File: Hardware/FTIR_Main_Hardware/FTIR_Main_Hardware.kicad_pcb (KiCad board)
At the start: 2 copper layers, 85.9 x 53.1 mm, 52 parts, among them J1 RJ45_LED_Shielded, Q1 IRF7606PBF, Q2 BSS138, Q3 IRF7606PBF, Q4 IRF7606PBF, Q5 BSS138, Q6 BSS138, U2 D36V28F7, U3 OKI, U4 TMC2208_Breakout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

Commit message: Added a few traces
I have an 8 AM class in 5 hours :(
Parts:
- C1, C2, C4, C5: moved to B.Cu
- moved C5 9.42 mm to (133.6, 82.8)
- moved C1 6.41 mm to (121.2, 82.8), turned to 180 degrees
- moved C4 6.24 mm to (133.6, 87.9), turned to 0 degrees
- moved C2 5.05 mm to (121.2, 87.9)
- moved R12 0.61 mm to (134.4, 78.3)
- moved Q2 0.48 mm to (131.3, 78.3)
- moved R11 0.48 mm to (128.3, 76.0), turned to -90 degrees
- moved R10 0.48 mm to (131.2, 75.1)
- moved Q1 0.46 mm to (130.1, 70.2)
- moved D9 0.45 mm to (144.3, 72.3)
- moved R19 0.45 mm to (144.3, 68.5)
- moved R21 0.35 mm to (144.2, 78.5)
- moved R9 0.29 mm to (134.2, 68.5)
- moved D7 0.29 mm to (134.2, 72.3)
- moved D10 0.29 mm to (154.4, 72.2)
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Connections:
- Conn1 pad 2: (no net) -> +12V
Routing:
- net +12V: track 0.00 -> 96.5 mm
- net +7.5V: track 0.00 -> 93.6 mm, vias 0 -> 1
- net +5V: track 0.00 -> 68.0 mm
- net T-: track 0.00 -> 54.3 mm
- net T+: track 0.00 -> 54.2 mm
- net R+: track 0.00 -> 53.5 mm
- net R-: track 0.00 -> 53.4 mm
- net +3V3: track 0.00 -> 39.8 mm
- net Net-(Conn12-Pad1): track 0.00 -> 11.1 mm
- net Net-(Conn6-Pad1): track 0.00 -> 10.9 mm
- net Net-(C3-Pad1): track 0.00 -> 10.6 mm
- net Net-(Conn11-Pad1): track 0.00 -> 10.3 mm
- net Net-(Conn4-Pad4): track 0.00 -> 10.3 mm
- net Net-(Conn4-Pad1): track 0.00 -> 10.3 mm
- net Net-(Conn4-Pad3): track 0.00 -> 10.3 mm
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
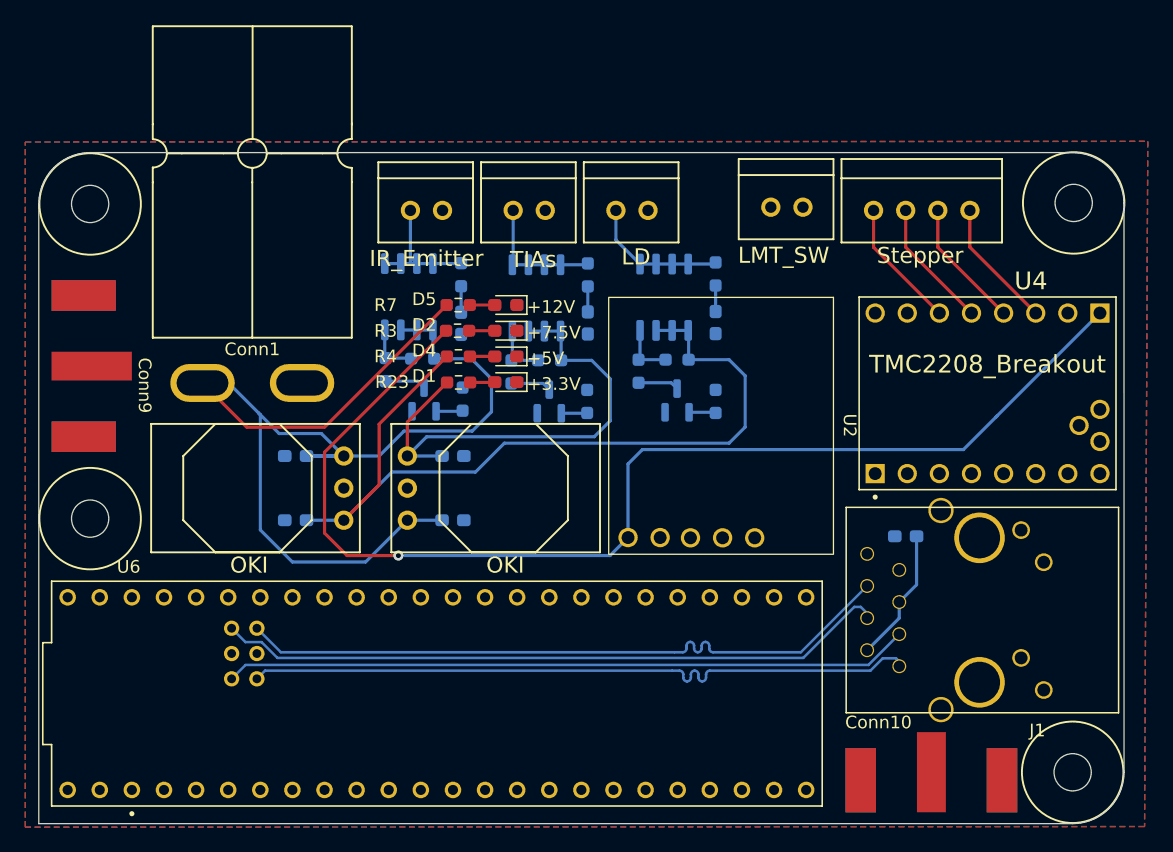
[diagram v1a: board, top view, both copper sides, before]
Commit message: More trace routing
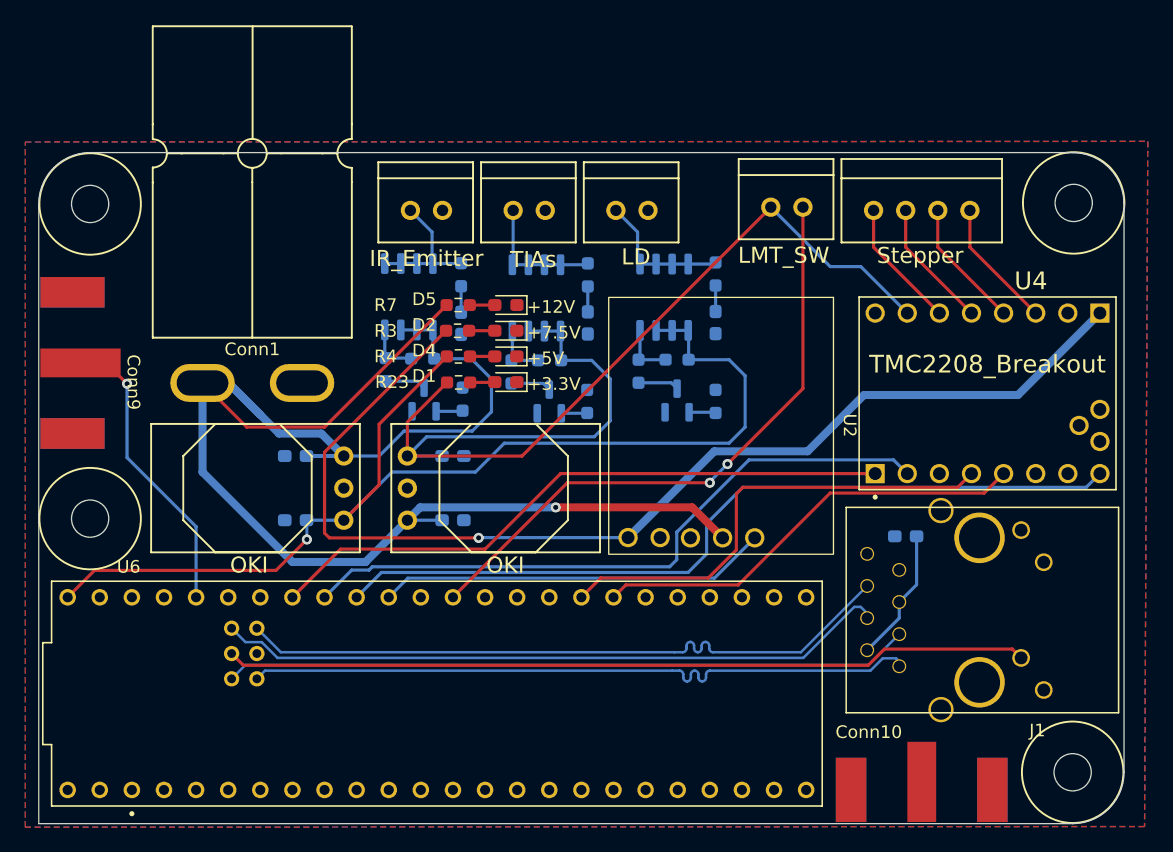
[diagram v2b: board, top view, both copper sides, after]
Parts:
- moved Conn10 1.08 mm to (170.7, 109.2)
- moved Conn9 0.92 mm to (103.5, 75.4)
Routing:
- net DRIVER_EN: track 0.00 -> 64.3 mm
- net ETH_LED: track 0.00 -> 63.7 mm
- net STEP: track 0.00 -> 52.3 mm
- net +3V3: track 39.8 -> 90.9 mm
- net DIR: track 0.00 -> 50.2 mm
- net Net-(U6-A0): track 0.00 -> 48.9 mm, vias 0 -> 2
- net PDN: track 0.00 -> 37.5 mm
- net +12V: track 96.5 -> 132.9 mm, vias 0 -> 1
- net UART: track 0.00 -> 34.9 mm
- net BUCK_EN: track 0.00 -> 30.9 mm
- net Net-(Conn9-Tip): track 0.00 -> 23.5 mm, vias 0 -> 1
- net +5V: track 68.0 -> 90.4 mm, vias 0 -> 1
- net +7.5V: track 93.6 -> 88.9 mm

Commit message: Finished the board
Added traces and reassigned pins
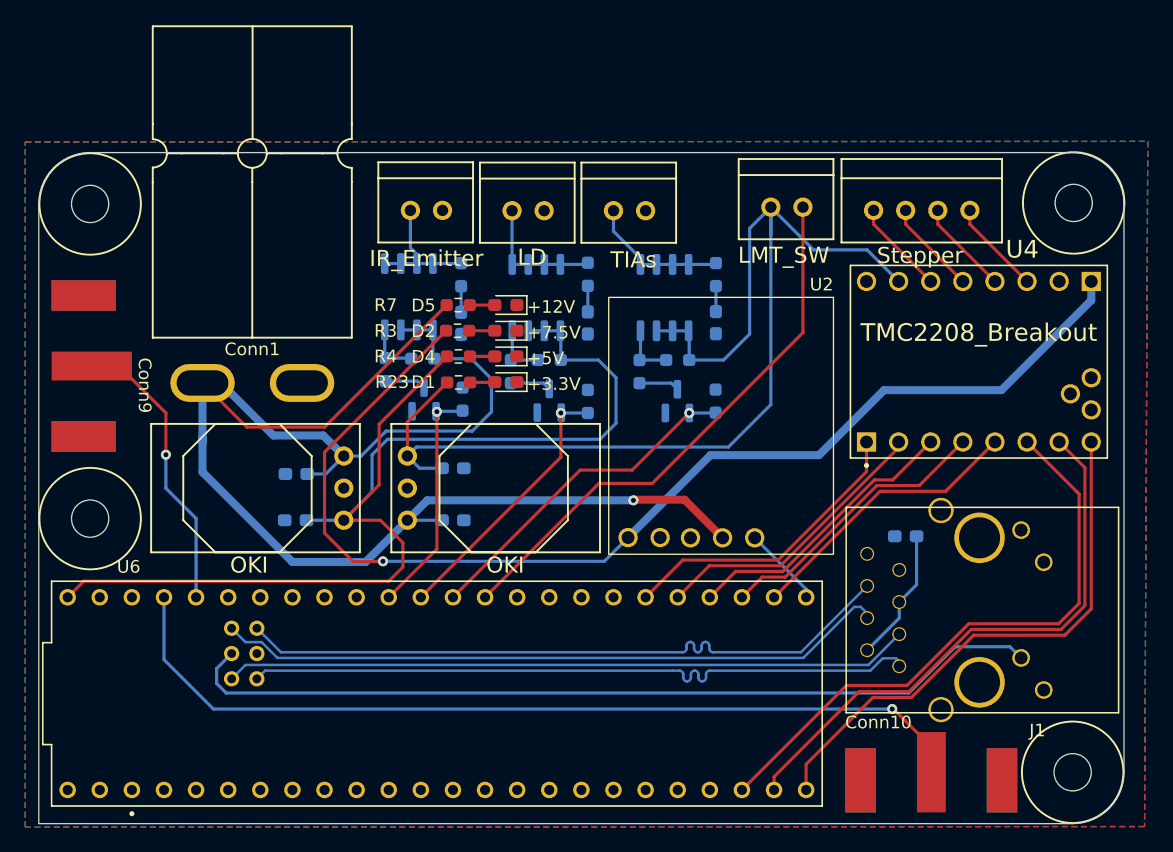
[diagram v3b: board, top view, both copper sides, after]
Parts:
- moved R21 10.2 mm to (154.4, 78.5)
- moved D9 10.1 mm to (154.4, 72.3)
- moved Q5 10.1 mm to (151.4, 78.5)
- moved R19 10.1 mm to (154.4, 68.5)
- moved Q3 10.1 mm to (150.3, 70.3)
- moved R15 10.1 mm to (151.4, 75.2)
- moved R17 10.1 mm to (148.4, 76.1)
- moved D10 10.1 mm to (144.3, 72.3)
- moved Q6 10.1 mm to (141.2, 78.4)
- moved R16 10.1 mm to (141.2, 75.2)
- moved R18 10.1 mm to (138.2, 76.1)
- moved R20 10.1 mm to (144.3, 68.4)
- moved Q4 10.1 mm to (140.2, 70.3)
- moved R22 10.1 mm to (144.3, 78.5)
- moved Conn12 8.22 mm to (138.3, 63.4)
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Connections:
- Conn1 pad 2: +12V -> (no net)
- Conn8 pad 2: Net-(U6-A0) -> Net-(U6-SCK)
- U6 pad 0: LAMP_CTRL -> unconnected-(U6-RX1-Pad0)
- U6 pad 1: MS1_CTRL -> unconnected-(U6-TX1-Pad1)
- U6 pad 13: unconnected-(U6-SCK-Pad13) -> Net-(U6-SCK)
- U6 pad 14: Net-(U6-A0) -> TIA_CTRL
- U6 pad 15: unconnected-(U6-A1-Pad15) -> LD_CTRL
- U6 pad 16: BUCK_EN -> LAMP_CTRL
- U6 pad 17: DRIVER_EN -> unconnected-(U6-A3-Pad17)
- U6 pad 18: STEP -> unconnected-(U6-A4-Pad18)
- U6 pad 19: DIR -> unconnected-(U6-A5-Pad19)
- U6 pad 2: MS2_CTRL -> unconnected-(U6-OUT2-Pad2)
- U6 pad 28: CLK -> unconnected-(U6-RX7-Pad28)
- U6 pad 30: unconnected-(U6-CRX3-Pad30) -> MS2_CTRL
- U6 pad 31: unconnected-(U6-CTX3-Pad31) -> MS1_CTRL
- U6 pad 32: unconnected-(U6-OUT1B-Pad32) -> DRIVER_EN
- U6 pad 33: unconnected-(U6-MCLK2-Pad33) -> BUCK_EN
- U6 pad 34: unconnected-(U6-RX8-Pad34) -> UART
- U6 pad 35: unconnected-(U6-TX8-Pad35) -> UART
- U6 pad 36: unconnected-(U6-CS2-Pad36) -> CLK
- U6 pad 37: unconnected-(U6-CS3-Pad37) -> STEP
- U6 pad 38: unconnected-(U6-A14-Pad38) -> DIR
- U6 pad 39: UART -> unconnected-(U6-A15-Pad39)
- U6 pad 40: PDN -> unconnected-(U6-A16-Pad40)
- U6 pad 7: TIA_CTRL -> unconnected-(U6-RX2-Pad7)
- U6 pad 8: LD_CTRL -> unconnected-(U6-TX2-Pad8)
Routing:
- net Net-(Conn10-Tip): track 0.00 -> 70.5 mm, vias 0 -> 1
- net Net-(U6-A0): track 48.9 -> 0.00 mm, vias 2 -> 0
- net MS2_CTRL: track 0.00 -> 47.3 mm
- net MS1_CTRL: track 0.00 -> 45.0 mm
- net Net-(U6-SCK): track 0.00 -> 43.7 mm
- net PDN: track 37.5 -> 0.00 mm
- net STEP: track 52.3 -> 22.8 mm
- net DIR: track 50.2 -> 23.9 mm
- net TIA_CTRL: track 2.06 -> 26.8 mm, vias 0 -> 1
- net BUCK_EN: track 30.9 -> 6.39 mm
- net CLK: track 0.00 -> 22.6 mm
- net DRIVER_EN: track 64.3 -> 42.9 mm
- net LD_CTRL: track 2.12 -> 21.4 mm, vias 0 -> 1
- net LAMP_CTRL: track 2.12 -> 18.4 mm, vias 0 -> 1
- net UART: track 34.9 -> 45.1 mm
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
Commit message: Finishing touches on all boards
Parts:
- added G***: LOGO, LOGO, B.Cu at (159.8, 73.5)
- added G***: LOGO, LOGO, B.Cu at (118.0, 69.7)
- added G***: LOGO, LOGO, B.Cu at (147.5, 91.7)
- moved Conn9 0.89 mm to (103.5, 75.7)
- moved Conn10 0.64 mm to (171.4, 109.1)
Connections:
- Conn1 pad 2: (no net) -> +12V
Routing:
- net unconnected-(U6-3.3V-Pad3.3V_1): track 0.00 -> 39.9 mm
- net +12V: track 132.0 -> 127.7 mm
- net Net-(Conn10-Tip): track 70.5 -> 73.2 mm
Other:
- board text added: "7.5v Buck"
- board text added: "FTIR Spectrometer, Rev1 Mars Rover Design Team Missouri S&T, 2024 Drew Wellen and Adam Klassen"

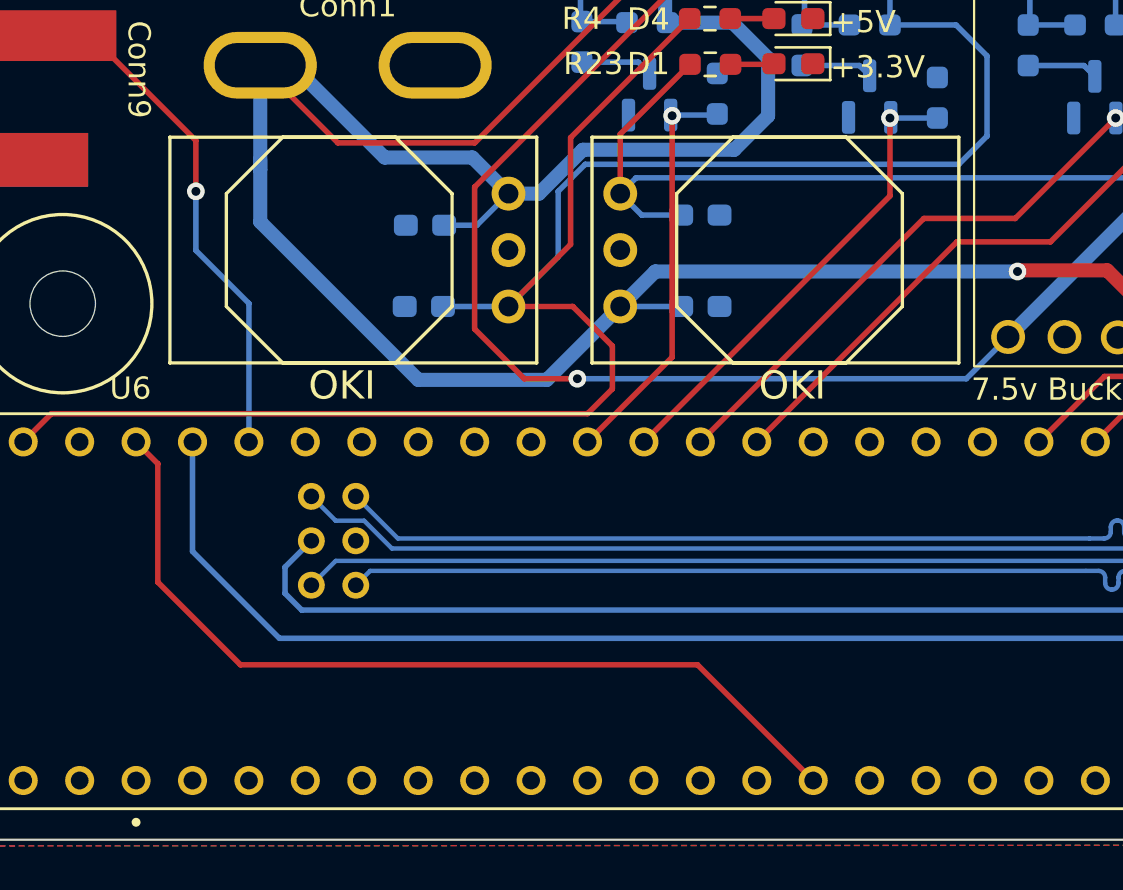
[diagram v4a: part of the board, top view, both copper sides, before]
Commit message: Tweaked one trace
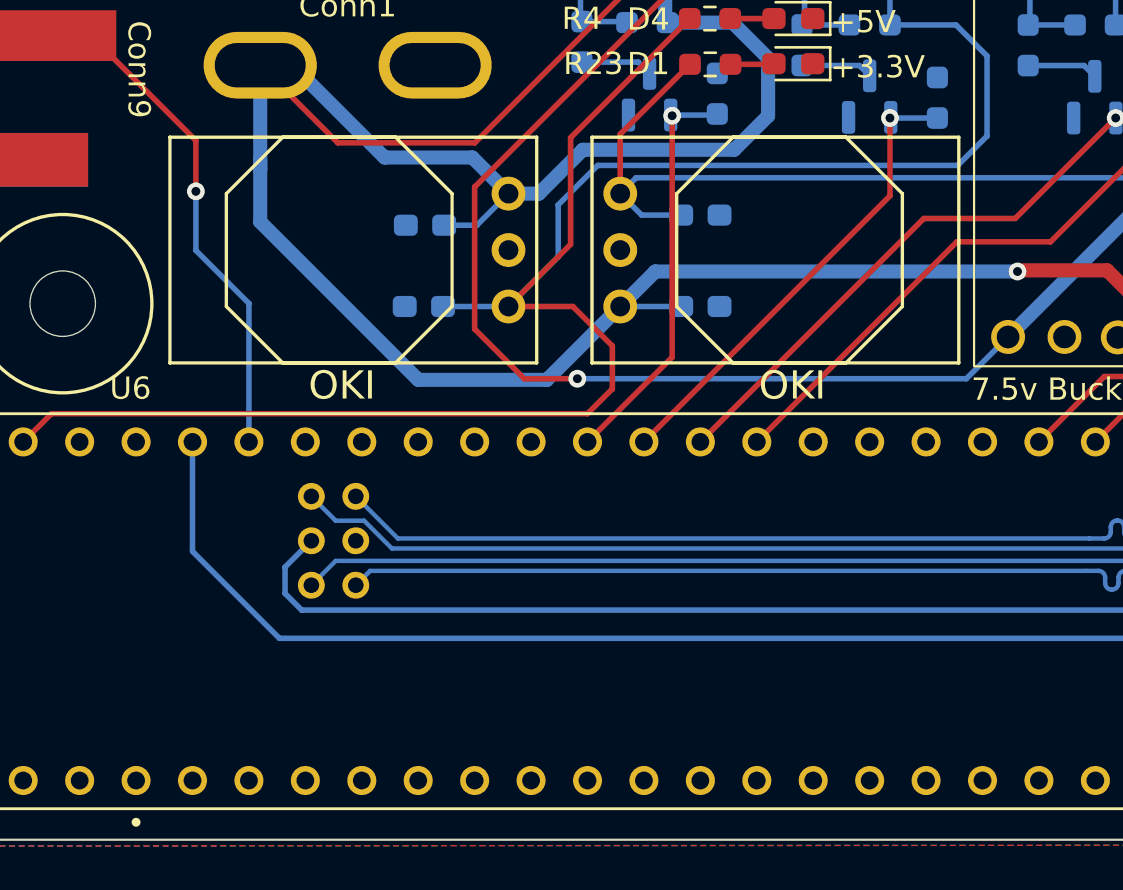
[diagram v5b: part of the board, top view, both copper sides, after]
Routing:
- net unconnected-(U6-3.3V-Pad3.3V_1): track 39.9 -> 0.00 mm
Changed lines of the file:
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@@
   (segment (start 127.762 85.09) (end 127.762 80.285926) (width 0.25) (layer "F.Cu") (net 3))
   (segment (start 129.6416 89.662) (end 129.6416 91.5924) (width 0.25) (layer "F.Cu") (net 3))
+  (segment (start 146.5072 80.2132) (end 146.5072 76.6064) (width 0.25) (layer "B.Cu") (net 3))
   (segment (start 139.5628 72.8957) (end 142.1028 72.8957) (width 0.25) (layer "B.Cu") (net 3))
-  (segment (start 145.1125 75.2117) (end 142.1384 75.2117) (width 0.25) (layer "B.Cu") (net 3))
   (segment (start 142.1384 72.9313) (end 142.1028 72.8957) (width 0.25) (layer "B.Cu") (net 3))
   (segment (start 124.968 87.884) (end 122.0205 87.884) (width 0.25) (layer "B.Cu") (net 3))
-  (segment (start 127.2032 85.6488) (end 127.2032 82.7024) (width 0.25) (layer "B.Cu") (net 3))
+  (segment (start 128.9812 81.534) (end 145.1864 81.534) (width 0.25) (layer "B.Cu") (net 3))
+  (segment (start 145.1125 75.2117) (end 142.1384 75.2117) (width 0.25) (layer "B.Cu") (net 3))
+  (segment (start 124.968 87.884) (end 127.2032 85.6488) (width 0.25) (layer "B.Cu") (net 3))
+  (segment (start 142.1384 75.2117) (end 142.1384 72.9313) (width 0.25) (layer "B.Cu") (net 3))
+  (segment (start 127.2032 85.6488) (end 127.2032 83.312) (width 0.25) (layer "B.Cu") (net 3))
+  (segment (start 145.1864 81.534) (end 146.5072 80.2132) (width 0.25) (layer "B.Cu") (net 3))
+  (segment (start 127.2032 83.312) (end 128.9812 81.534) (width 0.25) (layer "B.Cu") (net 3))
   (segment (start 146.5072 76.6064) (end 145.1125 75.2117) (width 0.25) (layer "B.Cu") (net 3))
-  (segment (start 146.5072 80.2132) (end 146.5072 76.6064) (width 0.25) (layer "B.Cu") (net 3))
-  (segment (start 127.2032 82.7024) (end 128.4224 81.4832) (width 0.25) (layer "B.Cu") (net 3))
-  (segment (start 142.1384 75.2117) (end 142.1384 72.9313) (width 0.25) (layer "B.Cu") (net 3))
-  (segment (start 124.968 87.884) (end 127.2032 85.6488) (width 0.25) (layer "B.Cu") (net 3))
-  (segment (start 145.2372 81.4832) (end 146.5072 80.2132) (width 0.25) (layer "B.Cu") (net 3))
-  (segment (start 128.4224 81.4832) (end 145.2372 81.4832) (width 0.25) (layer "B.Cu") (net 3))
   (segment (start 170.2805 92.985213) (end 168.91 94.355713) (width 0.25) (layer "B.Cu") (net 4))
   (segment (start 170.2805 89.154) (end 170.2805 92.985213) (width 0.25) (layer "B.Cu") (net 4))
@@
   (segment (start 183.1412 94.454004) (end 183.1412 85.8084) (width 0.25) (layer "F.Cu") (net 39))
   (segment (start 169.531602 100.951602) (end 174.408402 96.074802) (width 0.25) (layer "F.Cu") (net 39))
-  (segment (start 133.477 104.013) (end 138.684 109.22) (width 0.25) (layer "F.Cu") (net 41))
-  (segment (start 109.183 100.293) (end 112.903 104.013) (width 0.25) (layer "F.Cu") (net 41))
-  (segment (start 112.903 104.013) (end 133.477 104.013) (width 0.25) (layer "F.Cu") (net 41))
-  (segment (start 109.183 94.959) (end 109.183 100.293) (width 0.25) (layer "F.Cu") (net 41))
-  (segment (start 108.204 93.98) (end 109.183 94.959) (width 0.25) (layer "F.Cu") (net 41))
   (segment (start 157.474713 89.275713) (end 161.544 93.345) (width 0.25) (layer "B.Cu") (net 51))
   (segment (start 161.544 93.345) (end 161.544 93.98) (width 0.25) (layer "B.Cu") (net 51))

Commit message: Fixed some things from the layout
haha drew and ethan can't stop me anymore
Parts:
- removed C4, C5: 10uF, Capacitor_SMD:C_0603_1608Metric_Pad1.08x0.95mm_HandSolder
- removed Conn11: TIAs, MRDT_Connectors:MOLEX_SL_02_Vertical
- removed D1, D9: Green, LED_SMD:LED_0603_1608Metric_Pad1.05x0.95mm_HandSolder
- removed Q3: IRF7606PBF, Package_SO:SOP-8_3.9x4.9mm_P1.27mm
- removed Q5: BSS138, Package_TO_SOT_SMD:SOT-23
- removed R15: 10k, Resistor_SMD:R_0603_1608Metric_Pad0.98x0.95mm_HandSolder
- removed R17: 3.3k, Resistor_SMD:R_0603_1608Metric_Pad0.98x0.95mm_HandSolder
- removed R19, R23: 100, Resistor_SMD:R_0603_1608Metric_Pad0.98x0.95mm_HandSolder
- removed R21: 4.7k, Resistor_SMD:R_0603_1608Metric_Pad0.98x0.95mm_HandSolder
- removed U7: OKI, MRDT_Devices:OKI_Horizontal
- added Conn2: LMT_SW_2, MRDT_Connectors:MOLEX_SL_02_Vertical, F.Cu at (151.0, 63.3)
- added Conn3: TIAs, MRDT_Connectors:MOLEX_SL_02_Vertical, F.Cu at (135.3, 84.3)
- added R1: 4.7k, Resistor_SMD:R_0603_1608Metric_Pad0.98x0.95mm_HandSolder, F.Cu at (159.3, 68.9)
- added R2: 4.7k, Resistor_SMD:R_0603_1608Metric_Pad0.98x0.95mm_HandSolder, F.Cu at (151.3, 68.9)
- Conn8: value LMT_SW -> LMT_SW_1
- moved G*** 108.2 mm to (51.6, 73.0)
- moved G*** 86.4 mm to (61.1, 88.8)
- moved G*** 58.5 mm to (60.4, 59.4)
- moved Conn4 1.12 mm to (168.0, 63.3)
- moved Conn8 0.27 mm to (159.0, 63.3)
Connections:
- Conn1 pad 2: +12V -> (no net)
- Conn8 pad 2: Net-(U6-SCK) -> Net-(U6-A16)
- U6 pad 13: Net-(U6-SCK) -> LD_CTRL
- U6 pad 14: TIA_CTRL -> LAMP_CTRL
- U6 pad 15: LD_CTRL -> unconnected-(U6-A1-Pad15)
- U6 pad 16: LAMP_CTRL -> unconnected-(U6-A2-Pad16)
- U6 pad 3.3V_1: unconnected-(U6-3.3V-Pad3.3V_1) -> +3V3
- U6 pad 3.3V_2: unconnected-(U6-3.3V-Pad3.3V_1) -> +3V3
- U6 pad 40: unconnected-(U6-A16-Pad40) -> Net-(U6-A16)
- U6 pad 41: unconnected-(U6-A17-Pad41) -> Net-(U6-A17)
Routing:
- net +3V3: track 92.3 -> 192.7 mm
- net Net-(U6-A16): track 0.00 -> 47.4 mm
- net Net-(U6-SCK): track 43.7 -> 0.00 mm
- net Net-(U6-A17): track 0.00 -> 41.9 mm
- net TIA_CTRL: track 26.8 -> 0.00 mm, vias 1 -> 0
- net Net-(Conn11-Pad1): track 11.2 -> 0.00 mm
- net +12V: track 127.7 -> 122.9 mm
- net Net-(Q3-G): track 4.46 -> 0.00 mm
- net Net-(Q5-D): track 3.20 -> 0.00 mm
- net LD_CTRL: track 21.4 -> 19.3 mm
- net Net-(D9-A): track 2.01 -> 0.00 mm
- net Net-(D1-A): track 1.96 -> 0.00 mm
- net LAMP_CTRL: track 18.4 -> 17.4 mm
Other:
- board text removed: "+3.3V"
